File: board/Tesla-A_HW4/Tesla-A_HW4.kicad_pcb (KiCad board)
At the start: 2 copper layers, 42 x 27 mm, 4 parts, among them J1 5016451220, J2 Conn_01x04_Pin

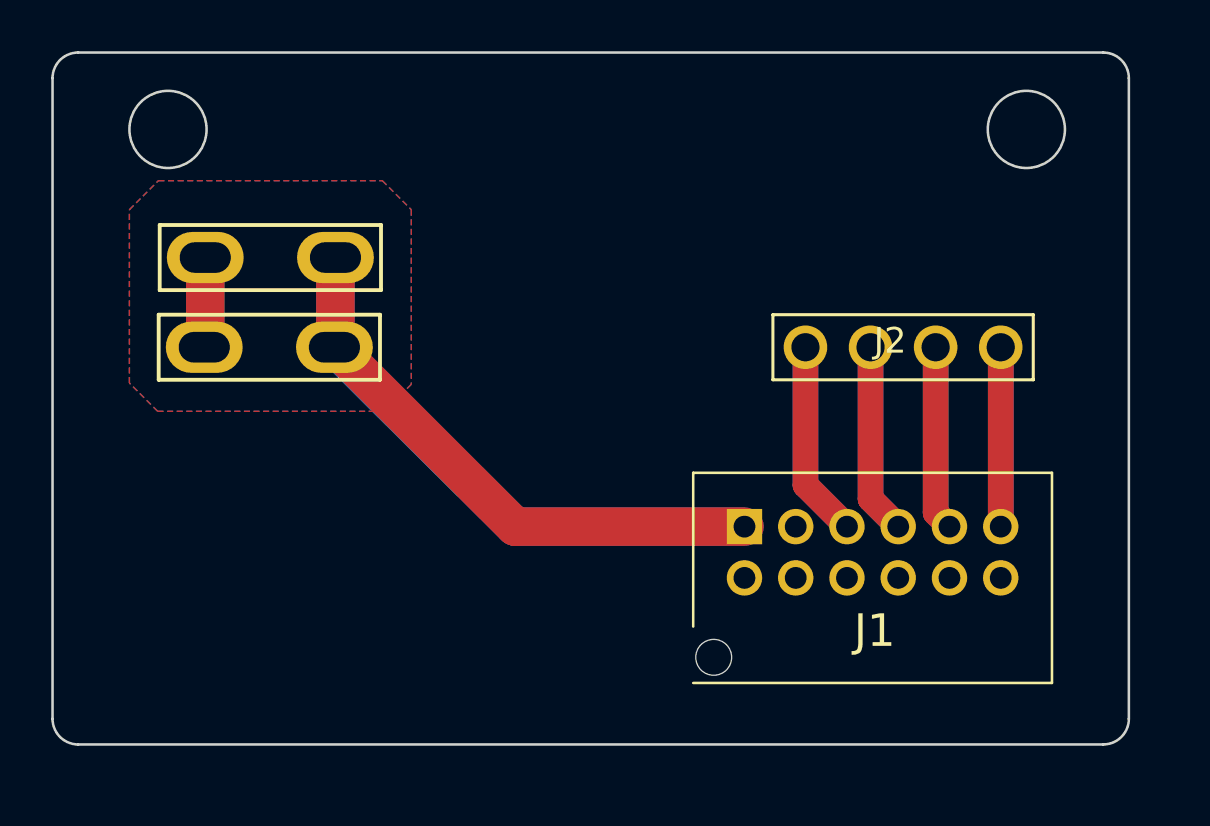
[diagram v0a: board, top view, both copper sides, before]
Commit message: add BYD-1, 2, 3, 4, 5, 6
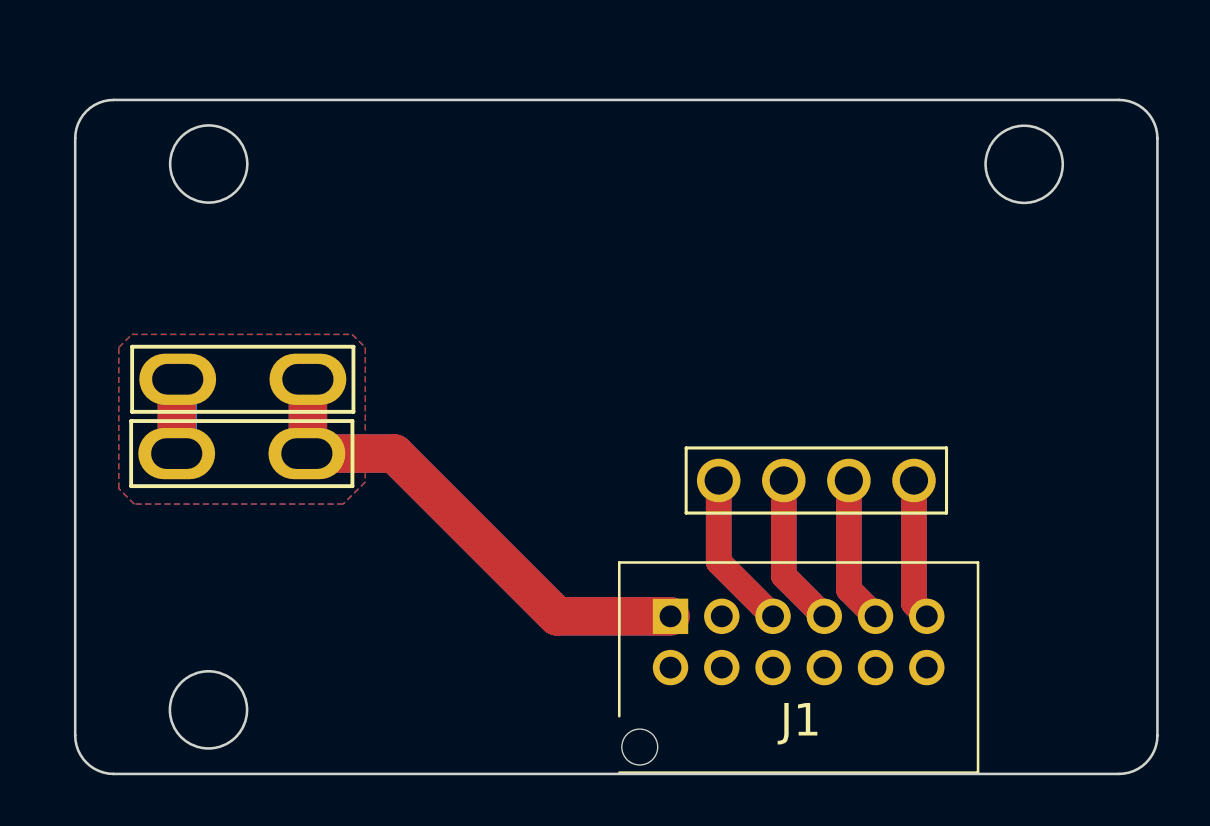
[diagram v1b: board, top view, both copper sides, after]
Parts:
- added G***: LOGO, LOGO, B.Cu at (153.5, 72.0)
- moved J2 6.20 mm to (157.6, 79.7)
- moved J3 4.87 mm to (128.9, 75.8)
- moved J1 4.54 mm to (148.1, 85.0)
- moved J3 4.29 mm to (128.8, 78.7)
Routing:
- net 12VIN: track 51.9 -> 45.4 mm
- net CAN0_H-OR: track 15.3 -> 12.4 mm
- net PT3: track 14.0 -> 11.0 mm
- net CAN0_L-GR: track 14.9 -> 11.9 mm
- net PT4: track 14.4 -> 11.5 mm
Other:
- board size 42 x 27 mm -> 42.2 x 26.3 mm
- board text added: "${CURRENT_DATE}"
- board text added: "Rev. ${REVISION}"
- board text added: "Tesla-B HW4 HARNESS"
